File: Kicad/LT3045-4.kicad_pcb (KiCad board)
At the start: 4 copper layers, 100 x 50 mm, 22 parts, among them J1 Conn_Coaxial_Power, J2 Conn_Coaxial_Power, U1 LT3042, U2 LT3042, U3 LT3042, U4 LT3042

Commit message: 1st design
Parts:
- moved C10 5.85 mm to (9.80, 22.0)
- moved L1 5.85 mm to (11.2, 25.0)
- moved C1 5.05 mm to (9.70, 30.9)
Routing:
- net GND: track 14.3 -> 29.9 mm
- net Net-(C1-Pad1): track 0.00 -> 11.7 mm

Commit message: 1st draft
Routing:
- net /VOUT: track 117.2 -> 136.6 mm, vias 13 -> 25
- net (no net): track 0.00 -> 19.2 mm
- net Net-(C2-Pad1): track 33.3 -> 34.0 mm
- net GND: vias 32 -> 44
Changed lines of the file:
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@@
     (thickness 1.6)
     (drawings 4)
-    (tracks 229)
+    (tracks 271)
     (zones 0)
     (modules 22)
@@
   (gr_line (start 0 50) (end 100 50) (layer Edge.Cuts) (width 0.05))
   (gr_line (start 100 0) (end 100 50) (layer Edge.Cuts) (width 0.05))
+  (segment (start 48.1 11.5) (end 48.1 9.1) (width 2) (layer B.Cu) (net 0))
+  (segment (start 45.8 20.8) (end 45.8 18.4) (width 2) (layer B.Cu) (net 0))
+  (segment (start 45.8 30.9) (end 45.8 28.5) (width 2) (layer B.Cu) (net 0))
+  (segment (start 48.1 41.2) (end 48.1 38.8) (width 2) (layer B.Cu) (net 0))
+  (segment (start 35.3 40.8) (end 35.3 38.4) (width 0.5) (layer B.Cu) (net 0))
+  (segment (start 38.1 33.1) (end 38.1 30.7) (width 0.5) (layer B.Cu) (net 0))
+  (segment (start 35 25.9) (end 35 23.5) (width 0.5) (layer B.Cu) (net 0))
+  (segment (start 38.4 18.5) (end 38.4 16.1) (width 0.5) (layer B.Cu) (net 0))
   (via (at 52.3 46.3) (size 0.8) (drill 0.4) (layers F.Cu B.Cu) (net 1))
   (segment (start 51 46.3) (end 52.3 46.3) (width 0.25) (layer F.Cu) (net 1))
@@
   (segment (start 4.95 29.25) (end 9.7 34) (width 0.25) (layer F.Cu) (net 1))
   (segment (start 3 29.25) (end 4.95 29.25) (width 0.25) (layer F.Cu) (net 1))
+  (via (at 86.2 28.9) (size 0.8) (drill 0.4) (layers F.Cu B.Cu) (net 1))
+  (via (at 86.3 21.2) (size 0.8) (drill 0.4) (layers F.Cu B.Cu) (net 1))
+  (via (at 64.3 12.9) (size 0.8) (drill 0.4) (layers F.Cu B.Cu) (net 1))
+  (via (at 64.6 19.7) (size 0.8) (drill 0.4) (layers F.Cu B.Cu) (net 1))
+  (via (at 64.4 30.4) (size 0.8) (drill 0.4) (layers F.Cu B.Cu) (net 1))
+  (via (at 64.7 37) (size 0.8) (drill 0.4) (layers F.Cu B.Cu) (net 1))
+  (via (at 64.6 25.5) (size 0.8) (drill 0.4) (layers F.Cu B.Cu) (net 1))
+  (via (at 64.5 28.7) (size 0.8) (drill 0.4) (layers F.Cu B.Cu) (net 1))
+  (via (at 64.5 21.2) (size 0.8) (drill 0.4) (layers F.Cu B.Cu) (net 1))
+  (via (at 64.5 23.6) (size 0.8) (drill 0.4) (layers F.Cu B.Cu) (net 1))
+  (via (at 59.5 40.4) (size 0.8) (drill 0.4) (layers F.Cu B.Cu) (net 1))
+  (via (at 58.8 7.8) (size 0.8) (drill 0.4) (layers F.Cu B.Cu) (net 1))
   (segment (start 3 25) (end 9.8 25) (width 1) (layer F.Cu) (net 2))
   (segment (start 9.8 22.9375) (end 9.8 25) (width 0.25) (layer F.Cu) (net 2))
@@
   (via (at 56.65 14.8) (size 0.8) (drill 0.4) (layers F.Cu B.Cu) (net 3))
   (segment (start 55.475 14.8) (end 56.65 14.8) (width 0.25) (layer F.Cu) (net 3))
-  (segment (start 56.8 43.8) (end 54.45 34.55) (width 1) (layer In1.Cu) (net 3))
   (via (at 54.35 24.05) (size 0.8) (drill 0.4) (layers F.Cu B.Cu) (net 3))
   (segment (start 54.45 34.55) (end 54.35 24.05) (width 1) (layer In1.Cu) (net 3))
   (segment (start 54.35 24.05) (end 56.65 14.8) (width 1) (layer In1.Cu) (net 3))
+  (segment (start 56.8 43.8) (end 56.8 38.7) (width 0.25) (layer In1.Cu) (net 3))
+  (segment (start 54.45 36.35) (end 54.45 34.55) (width 0.25) (layer In1.Cu) (net 3))
+  (segment (start 56.8 38.7) (end 54.45 36.35) (width 0.25) (layer In1.Cu) (net 3))
   (segment (start 49 26.25) (end 50.375 24.55) (width 0.25) (layer F.Cu) (net 4))
   (segment (start 83.25 24.75) (end 84.25 24.75) (width 0.25) (layer F.Cu) (net 5) (status 10))
@@
   (via (at 87.75 24.75) (size 0.8) (drill 0.4) (layers F.Cu B.Cu) (net 14))
   (segment (start 86.825 24.75) (end 87.75 24.75) (width 0.25) (layer F.Cu) (net 14) (status 10))
+  (via (at 55.5 12.6) (size 0.8) (drill 0.4) (layers F.Cu B.Cu) (net 14))
+  (via (at 55.5 11.8) (size 0.8) (drill 0.4) (layers F.Cu B.Cu) (net 14))
+  (via (at 55.5 11) (size 0.8) (drill 0.4) (layers F.Cu B.Cu) (net 14))
+  (segment (start 56 10.5) (end 55.5 11) (width 1) (layer In2.Cu) (net 14))
+  (segment (start 60 10.5) (end 56 10.5) (width 1) (layer In2.Cu) (net 14))
+  (via (at 53.2 21.8) (size 0.8) (drill 0.4) (layers F.Cu B.Cu) (net 14))
+  (via (at 53.2 21) (size 0.8) (drill 0.4) (layers F.Cu B.Cu) (net 14))
+  (via (at 53.2 20.2) (size 0.8) (drill 0.4) (layers F.Cu B.Cu) (net 14))
+  (via (at 53.2 32.4) (size 0.8) (drill 0.4) (layers F.Cu B.Cu) (net 14))
+  (via (at 53.2 31.6) (size 0.8) (drill 0.4) (layers F.Cu B.Cu) (net 14))
+  (via (at 53.2 30.8) (size 0.8) (drill 0.4) (layers F.Cu B.Cu) (net 14))
+  (via (at 55.5 41.6) (size 0.8) (drill 0.4) (layers F.Cu B.Cu) (net 14))
+  (via (at 55.5 40.8) (size 0.8) (drill 0.4) (layers F.Cu B.Cu) (net 14))
+  (via (at 55.5 40) (size 0.8) (drill 0.4) (layers F.Cu B.Cu) (net 14))
+  (segment (start 56 39.5) (end 55.5 40) (width 0.25) (layer In2.Cu) (net 14))
+  (segment (start 60 39.5) (end 56 39.5) (width 0.25) (layer In2.Cu) (net 14))
+  (segment (start 53.75 30.25) (end 53.2 30.8) (width 0.25) (layer In2.Cu) (net 14))
+  (segment (start 58 30.25) (end 53.75 30.25) (width 0.25) (layer In2.Cu) (net 14))
+  (segment (start 53.65 19.75) (end 53.2 20.2) (width 0.25) (layer In2.Cu) (net 14))
+  (segment (start 58 19.75) (end 53.65 19.75) (width 0.25) (layer In2.Cu) (net 14))
   (via (at 51.5 13.8) (size 0.8) (drill 0.4) (layers F.Cu B.Cu) (net 15))
   (segment (start 53.826998 16.2) (end 51.5 13.873002) (width 0.25) (layer In2.Cu) (net 15))
@@
       (pts
         (xy 87.25 20.5) (xy 86.5 22.625) (xy 85.75 24.75) (xy 86.5 28) (xy 87.25 29.75)
-        (xy 88.75 31.25) (xy 92.5 27.75) (xy 99.75 27.75) (xy 99.5 49.5) (xy 58.25 49.5)
-        (xy 58.25 0.5) (xy 99.5 0.5) (xy 99.75 24) (xy 98.875 23.125) (xy 98 22.25)
+        (xy 88.75 31.25) (xy 92.5 27.75) (xy 99.75 27.75) (xy 99.5 49.5) (xy 58.5 49.5)
+        (xy 58.3 0.5) (xy 99.5 0.5) (xy 99.75 24) (xy 98.875 23.125) (xy 98 22.25)
         (xy 92.5 22.25) (xy 88.75 18.5)
       )
@@
         (xy 53.1 11) (xy 54.8 11) (xy 54.8 17.4) (xy 54.4 17.8) (xy 52 17.8)
         (xy 50.8 19.1) (xy 50.8 20.3) (xy 52.7 20.3) (xy 52.7 24.8) (xy 51 24.8)
-        (xy 51 22.3) (xy 47.9 19.2) (xy 48.8 14.7) (xy 51.8 14.7) (xy 52.2 15.1)
+        (xy 51 22.3) (xy 47.7 19) (xy 48.8 14.7) (xy 51.8 14.7) (xy 52.2 15.1)
         (xy 53.1 15.1) (xy 53.1 12.8) (xy 51.7 11.4) (xy 50.3 10) (xy 49.1 10)
         (xy 49.1 8.1) (xy 54.5 8.1) (xy 53.1 9.5)

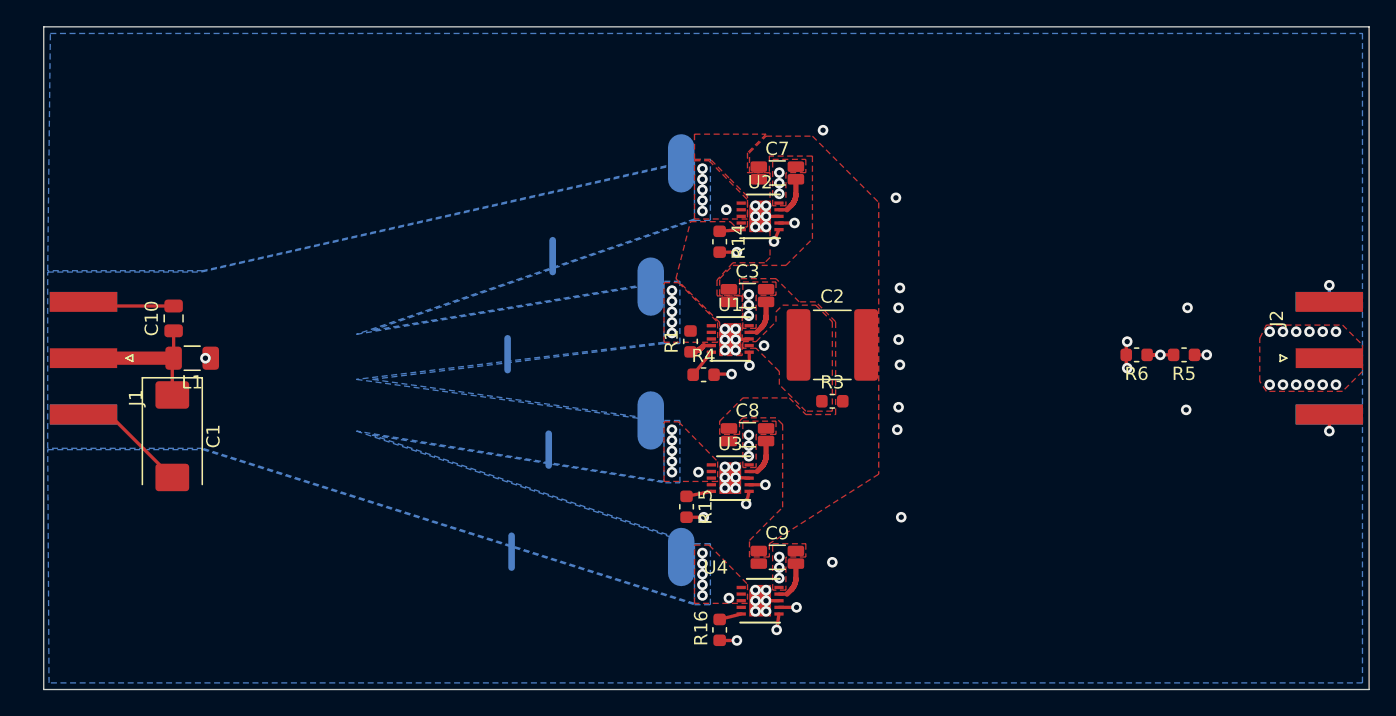
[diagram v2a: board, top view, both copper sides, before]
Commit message: Passed DRC minux pad to pad clearance
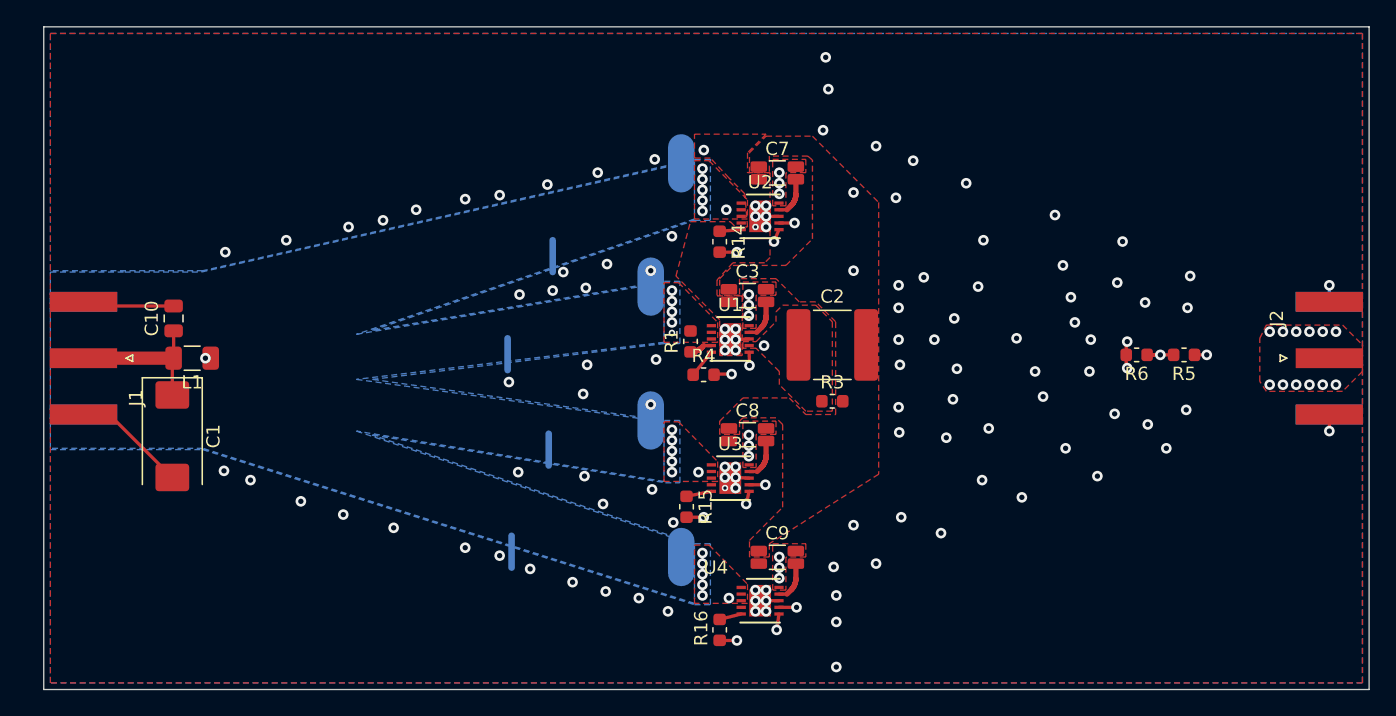
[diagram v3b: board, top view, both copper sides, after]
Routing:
- net GND: track 29.9 -> 49.1 mm, vias 44 -> 126
- net (no net): track 19.2 -> 0.00 mm
- added copper zone on In1.Cu, net Net-(C2-Pad1)
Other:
- net class Default: trace_width 0.25 -> 0.2; via_dia 0.8 -> 0.5; via_drill 0.4 -> 0.25
- rule via_min_drill: 0.3 -> 0.25
- rule via_min_size: 0.4 -> 0.5

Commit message: VIAS
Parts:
- added C11: 4.7µF 35V, Capacitor_SMD:C_0805_2012Metric, F.Cu at (58.1, 43.9)
- added C4: 4.7µF 35V, Capacitor_SMD:C_0805_2012Metric, F.Cu at (58.2, 14.8)
- added C5: 4.7µF 35V, Capacitor_SMD:C_0805_2012Metric, F.Cu at (56.0, 34.6)
- added C6: 4.7µF 35V, Capacitor_SMD:C_0805_2012Metric, F.Cu at (57.9, 29.3)
- moved R3 8.59 mm to (57.5, 19.9), turned to 90 degrees
- moved C2 0.50 mm to (59.5, 24.5)
- moved R4 0.27 mm to (49.5, 26.2), turned to 180 degrees
- moved R6 0.25 mm to (82.5, 25.0)
- moved R5 0.25 mm to (86.0, 25.0)
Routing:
- net GND: track 49.1 -> 119.0 mm, vias 126 -> 1066
- net Net-(C11-Pad1): track 34.0 -> 4.97 mm
- net /VOUT: track 136.6 -> 142.7 mm, vias 25 -> 38
- net Net-(R5-Pad2): track 34.9 -> 33.1 mm
- net /VIN: track 17.3 -> 17.0 mm, vias 27 -> 36
- added copper zone on In1.Cu, net GND
- added copper zone on F.Cu, net Net-(C1-Pad1)
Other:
- board text added: "Philippe Trottier"
